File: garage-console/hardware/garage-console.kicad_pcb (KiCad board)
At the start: 2 copper layers, 90 x 84 mm, 39 parts, among them J1 XH-2P, J10 XH-2P, J11 XH-2P, J12 XH-2P, J13 XH-2P, J14 XH-2P, J15 XH-2P, J16 XH-2P, J2 XH-2P, J3 XH-2P, J4 XH-2P, J5 XH-2P, J6 XH-2P, J7 XH-2P, J8 XH-2P, J9 XH-2P, U1 XIAO-ESP32-C6, U2 PCF8575

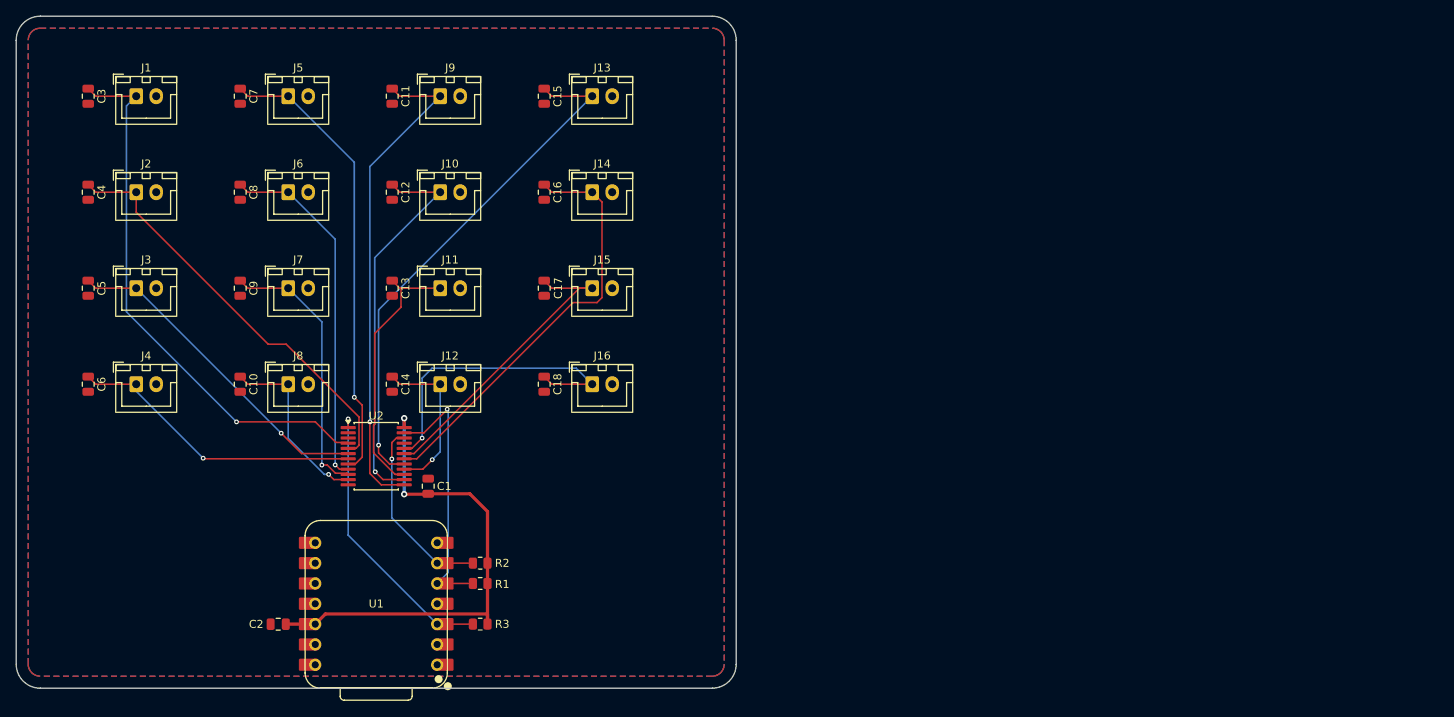
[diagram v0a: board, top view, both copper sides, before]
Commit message: garage-console: drop U1 footprint, correct header spacing, exclude THT headers from assembly
The XIAO module now has no schematic symbol or PCB footprint at all;
its real connections are carried entirely by HDR1/HDR2 (two 1x7
2.54mm female sockets), with the module's own male pins plugging in
by hand off-board. This avoids the permanent DRC parity warning a
zero-pad placeholder footprint produced. HDR1/HDR2 spacing was
corrected to 15.24mm (from Seeed's authoritative OPL library, the
prior extraction had picked up a cosmetic pad on one side and an
averaged position on the other), and both are now excluded from the
JLCPCB assembly BOM/CPL so they can be hand-soldered instead of
fighting an unresolved placement-rotation convention mismatch in the
assembly toolchain.

Also: project-local symbol library for the two named-pin header
symbols, filter cap mirror-symmetry fixes, and .gitignore now excludes
fab_export/ and jlcpcb/ (regenerable fabrication/assembly artifacts,
not source) plus stray calibration project files.
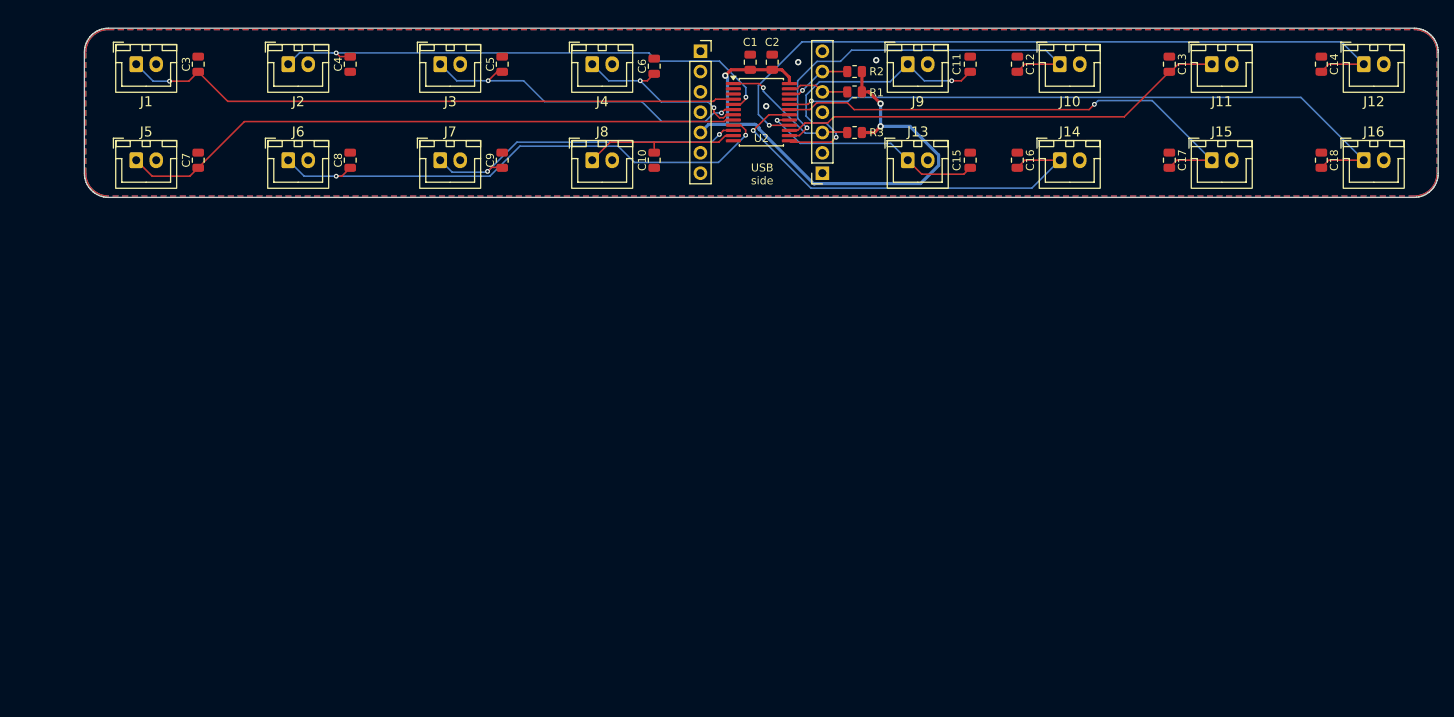
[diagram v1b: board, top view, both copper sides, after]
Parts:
- removed U1: XIAO-ESP32-C6, Seeed_Studio_XIAO_Series:XIAO-ESP32-C6-DIP
- added HDR1: Header_1x7_2.54mm, Connector_PinSocket_2.54mm:PinSocket_1x07_P2.54mm_Vertical, F.Cu at (100.8, 19.6)
- added HDR2: Header_1x7_2.54mm, Connector_PinSocket_2.54mm:PinSocket_1x07_P2.54mm_Vertical, F.Cu at (85.5, 4.38)
- moved C14 122.8 mm to (163.1, 6.00), turned to 90 degrees
- moved J12 122.2 mm to (168.4, 6.00)
- moved C13 101.1 mm to (144.1, 6.00), turned to 90 degrees
- moved C18 101.1 mm to (163.1, 18.0), turned to 90 degrees
- moved J11 100.4 mm to (149.4, 6.00)
- moved J16 100.4 mm to (168.4, 18.0)
- moved C2 93.5 mm to (94.5, 5.75), turned to 90 degrees
- moved C6 81.2 mm to (79.8, 6.25), turned to 90 degrees
- moved C17 79.8 mm to (144.1, 18.0), turned to 90 degrees
- moved C12 79.8 mm to (125.1, 6.00), turned to 90 degrees
- moved J10 79.1 mm to (130.4, 6.00)
- moved J15 79.1 mm to (149.4, 18.0)
- moved R1 77.2 mm to (104.8, 9.46)
- moved R2 77.2 mm to (104.8, 6.92)
- moved R3 77.2 mm to (104.8, 14.5)
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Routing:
- net /SW12: track 20.2 -> 92.8 mm
- net /SW16: track 39.3 -> 81.1 mm
- net /SW13: track 65.8 -> 28.8 mm
- net /SDA: track 33.5 -> 7.75 mm, vias 1 -> 0
- net /SW9: track 62.1 -> 37.4 mm, vias 1 -> 2
- net /SW15: track 38.5 -> 62.7 mm, vias 0 -> 1
- net /SW11: track 33.3 -> 56.2 mm
- net /SW6: track 44.8 -> 66.4 mm, vias 1 -> 2
- net /SW5: track 57.5 -> 78.4 mm, vias 1 -> 0
- net /PCF_INT: track 35.8 -> 17.1 mm
- net /SCL: track 23.7 -> 8.40 mm
- net /SW4: track 37.3 -> 23.0 mm, vias 1 -> 2
- net /SW2: track 52.4 -> 65.3 mm, vias 0 -> 2
- net /SW1: track 68.4 -> 77.7 mm
- net /SW7: track 34.0 -> 41.5 mm, vias 1 -> 2
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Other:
- board size 90 x 84 mm -> 169.2 x 21.1 mm
- board text added: "USB side"
